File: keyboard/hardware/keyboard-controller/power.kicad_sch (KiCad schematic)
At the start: 10 parts, among them J2 Barrel_Jack_Switch, U3 L78L09_TO92, U4 TL431, U5 LM1117-3.3

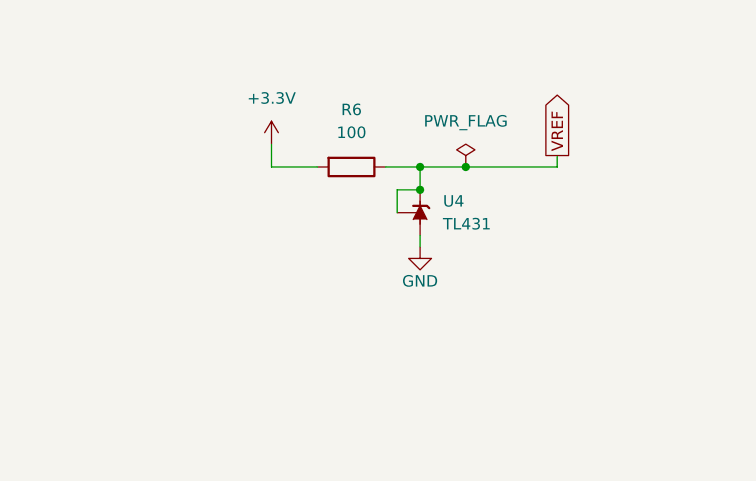
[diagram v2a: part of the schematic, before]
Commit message: Fixed wiring of keyboard connector, added TODOs
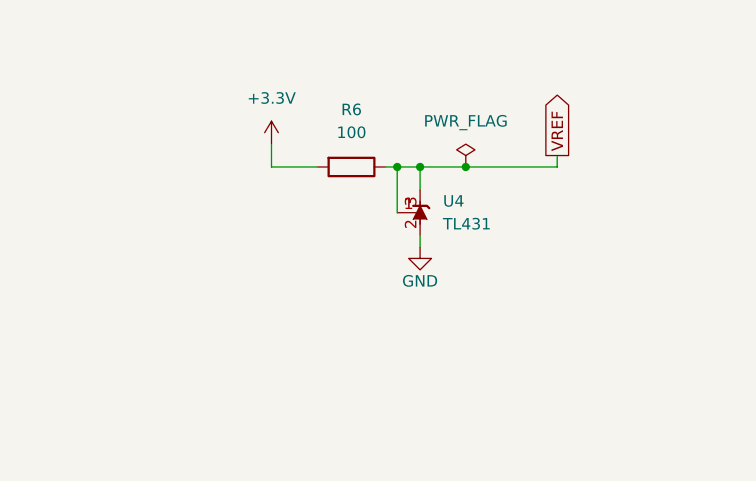
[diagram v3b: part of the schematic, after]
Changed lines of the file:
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@@
   (junction (at 96.52 116.84) (diameter 0) (color 0 0 0 0)
+  )
+  (junction (at 200.66 64.77) (diameter 0) (color 0 0 0 0)
   )
   (junction (at 191.77 115.57) (diameter 0) (color 0 0 0 0)
@@
   )
   (junction (at 208.28 124.46) (diameter 0) (color 0 0 0 0)
-  )
-  (junction (at 203.2 67.31) (diameter 0) (color 0 0 0 0)
   )
   (junction (at 90.17 62.23) (diameter 0) (color 0 0 0 0)
@@
     (stroke (width 0) (type default) (color 0 0 0 0))
   )
-  (wire (pts (xy 199.39 64.77) (xy 203.2 64.77))
+  (wire (pts (xy 199.39 64.77) (xy 200.66 64.77))
     (stroke (width 0) (type default) (color 0 0 0 0))
   )
@@
     (stroke (width 0) (type default) (color 0 0 0 0))
   )
-  (wire (pts (xy 191.77 116.84) (xy 191.77 115.57))
+  (wire (pts (xy 200.66 64.77) (xy 200.66 69.85))
     (stroke (width 0) (type default) (color 0 0 0 0))
   )
-  (wire (pts (xy 200.66 67.31) (xy 203.2 67.31))
+  (wire (pts (xy 191.77 116.84) (xy 191.77 115.57))
     (stroke (width 0) (type default) (color 0 0 0 0))
   )
@@
   )
   (wire (pts (xy 186.69 64.77) (xy 191.77 64.77))
-    (stroke (width 0) (type default) (color 0 0 0 0))
-  )
-  (wire (pts (xy 200.66 69.85) (xy 200.66 67.31))
     (stroke (width 0) (type default) (color 0 0 0 0))
   )
@@
     (stroke (width 0) (type default) (color 0 0 0 0))
   )
+  (wire (pts (xy 200.66 64.77) (xy 203.2 64.77))
+    (stroke (width 0) (type default) (color 0 0 0 0))
+  )

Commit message: Completed keyboard controller rev2
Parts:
- added SW1: SW_SPDT, Wealth_Metal_Switches:Slide_Switch_SPDT_SS12F44G5, symbol Switch:SW_SPDT
- added TP2: GND, TestPoint:TestPoint_Pad_D1.5mm, symbol Connector:TestPoint
- added TP3: +9V, TestPoint:TestPoint_Pad_D1.5mm, symbol Connector:TestPoint
- added TP4: +12V, TestPoint:TestPoint_Pad_D1.5mm, symbol Connector:TestPoint
- added TP5: VREF, TestPoint:TestPoint_Pad_D1.5mm, symbol Connector:TestPoint
- added TP6: 3.3V, TestPoint:TestPoint_Pad_D1.5mm, symbol Connector:TestPoint
- renumbered D6 to D5, R6 to R5
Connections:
- net +12V: now also SW1.1 (A), TP4.1; no longer J2.1
- net +3.3V: now also TP6.1
- net +9V: now also TP3.1
- net GND: now also TP2.1
- net VREF: now also TP5.1
- new net: J2.1, SW1.2 (B)
- no-connect marks 1 -> 2
